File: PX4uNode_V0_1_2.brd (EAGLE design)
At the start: 45.4 x 34 mm, 133 parts, among them J401 M04X2, M3_MOUNT1101 MOUNT-HOLE3.1MM, M3_MOUNT1102 MOUNT-HOLE3.1MM, M3_MOUNT1103 MOUNT-HOLE3.1MM, M3_MOUNT1104 MOUNT-HOLE3.1MM, U101 STM32F4X7VX, U401 MAX3051, U402 MAX3051, X101 3.2x2.5 mm / 24 MHz / 30 ppm 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

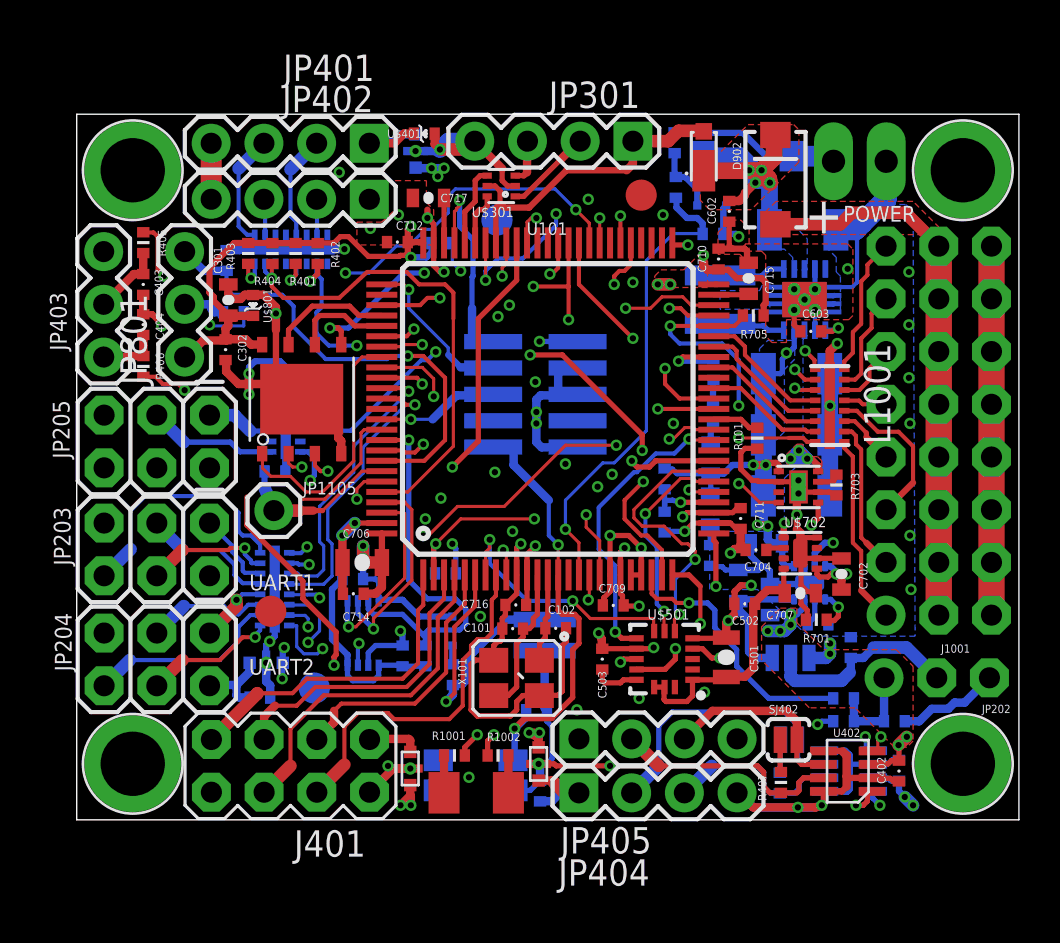
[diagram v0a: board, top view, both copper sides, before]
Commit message: Added uNode V0_1_2
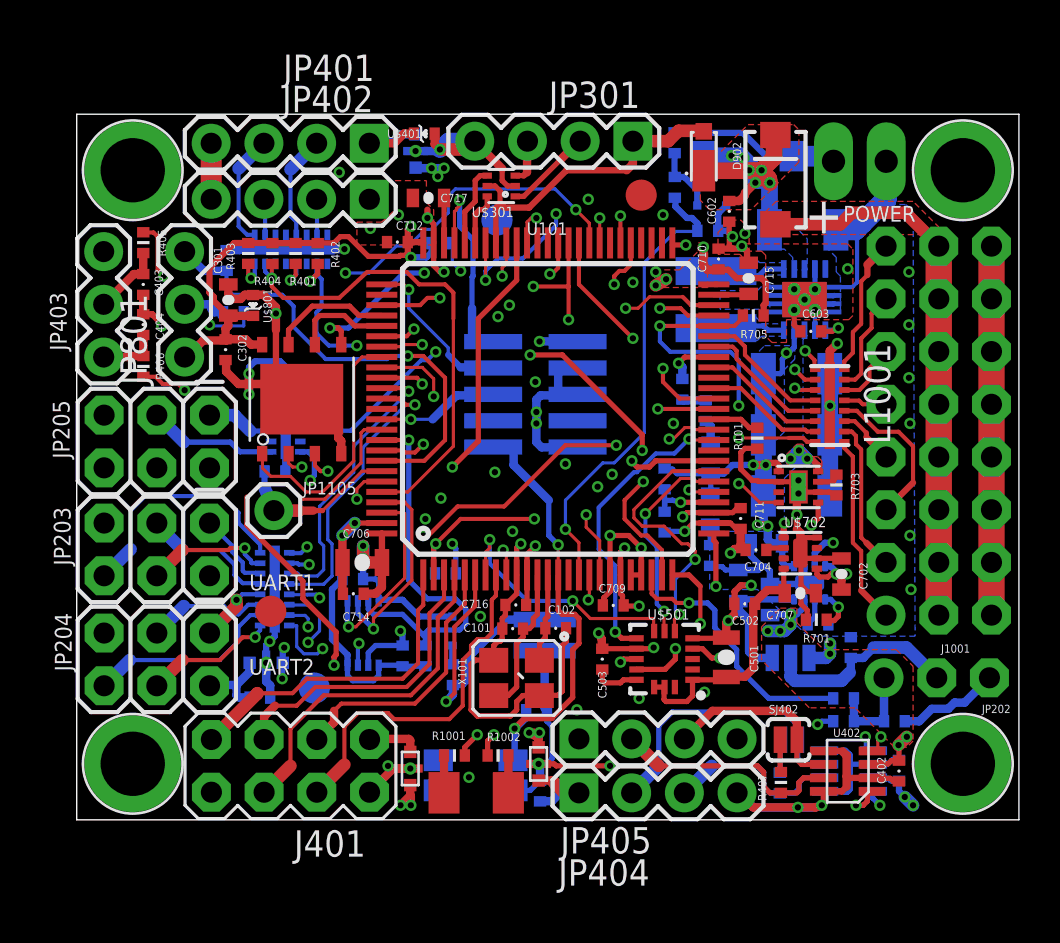
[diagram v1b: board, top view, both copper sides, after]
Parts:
- L$601: value XFL4020-222MEB -> IND_4X4_MULTI; device ti_tps_soln2:XFL4020 -> matts_lib:IND_4X4_MULTI
- moved R804 1.78 mm to (42.0, 24.9)
- moved R803 0.35 mm to (43.1, 23.9)
- moved R903 0.29 mm to (43.2, 32.6)
- moved L$601 0.20 mm to (43.6, 29.3)
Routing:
- net !VDD_5V_PERIPH_OC: track 16.9 -> 18.1 mm
- net !FMU-LED_AMBER: track 3.51 -> 2.65 mm
- net VDD_SERVO_SENSE: track 23.2 -> 22.6 mm
- net FMU-VDD_3V3: track 80.8 -> 81.2 mm, vias 21 -> 22
- net GND: vias 39 -> 41
- net VDD_IN: vias 4 -> 6
- added copper zone on layer 16, net N$10
- added copper zone on layer 16, net N$17
